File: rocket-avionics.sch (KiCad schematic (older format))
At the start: 20 parts

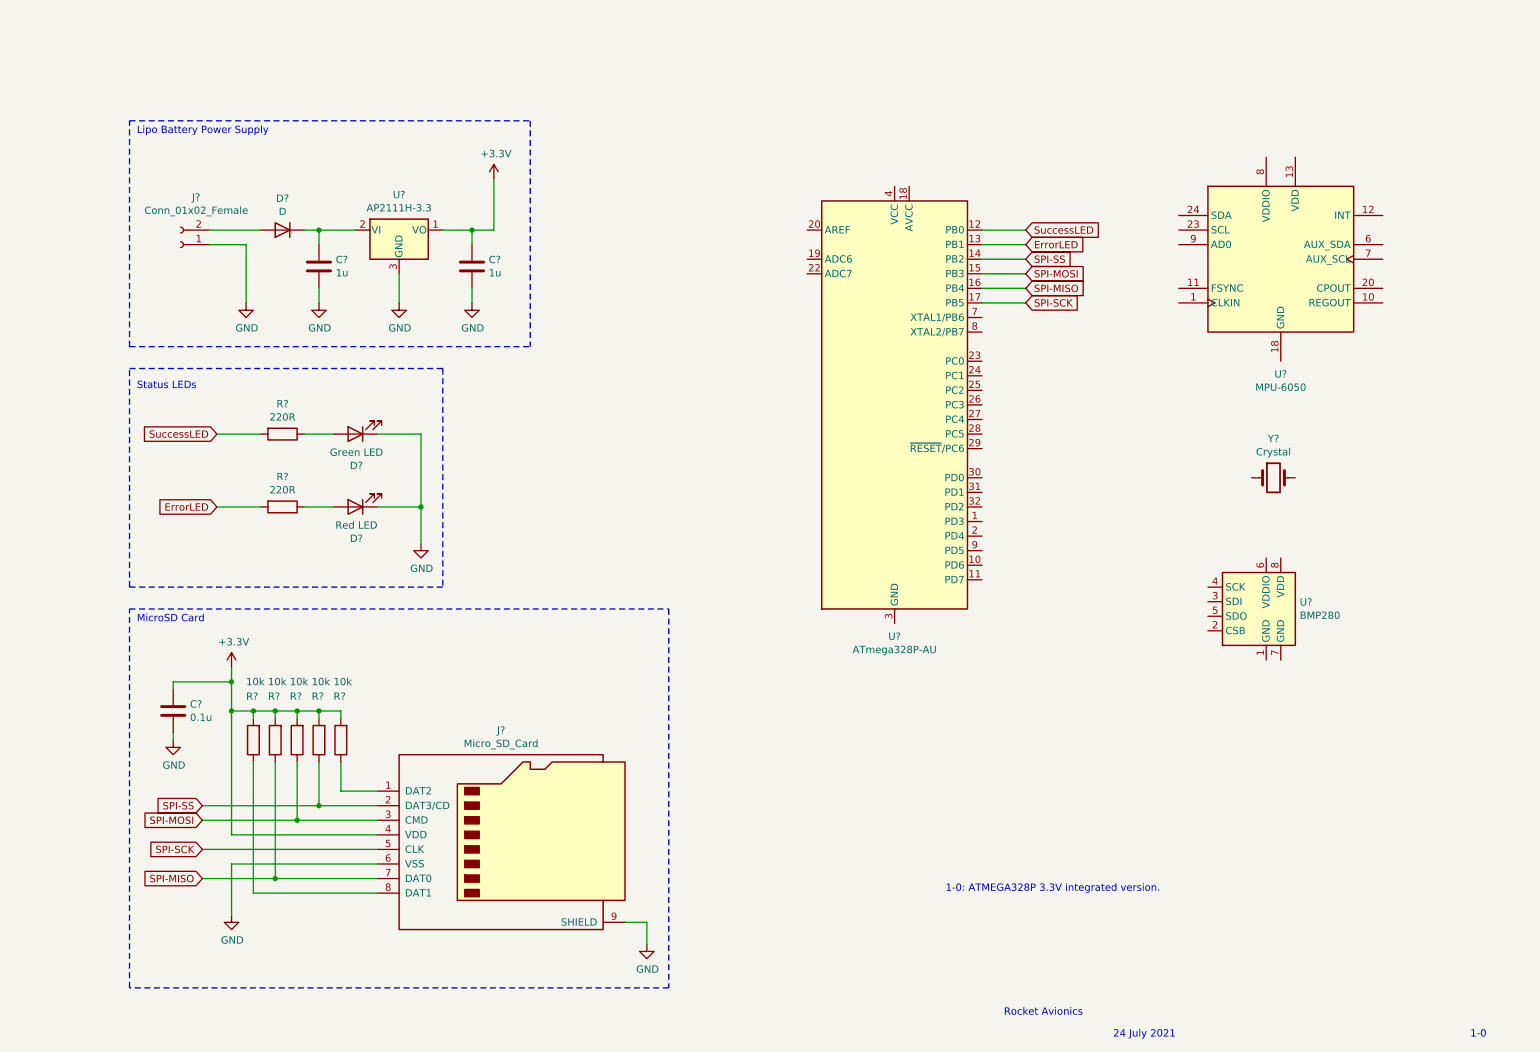
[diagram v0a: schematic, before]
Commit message: Complete MPU6050 section of schematic.
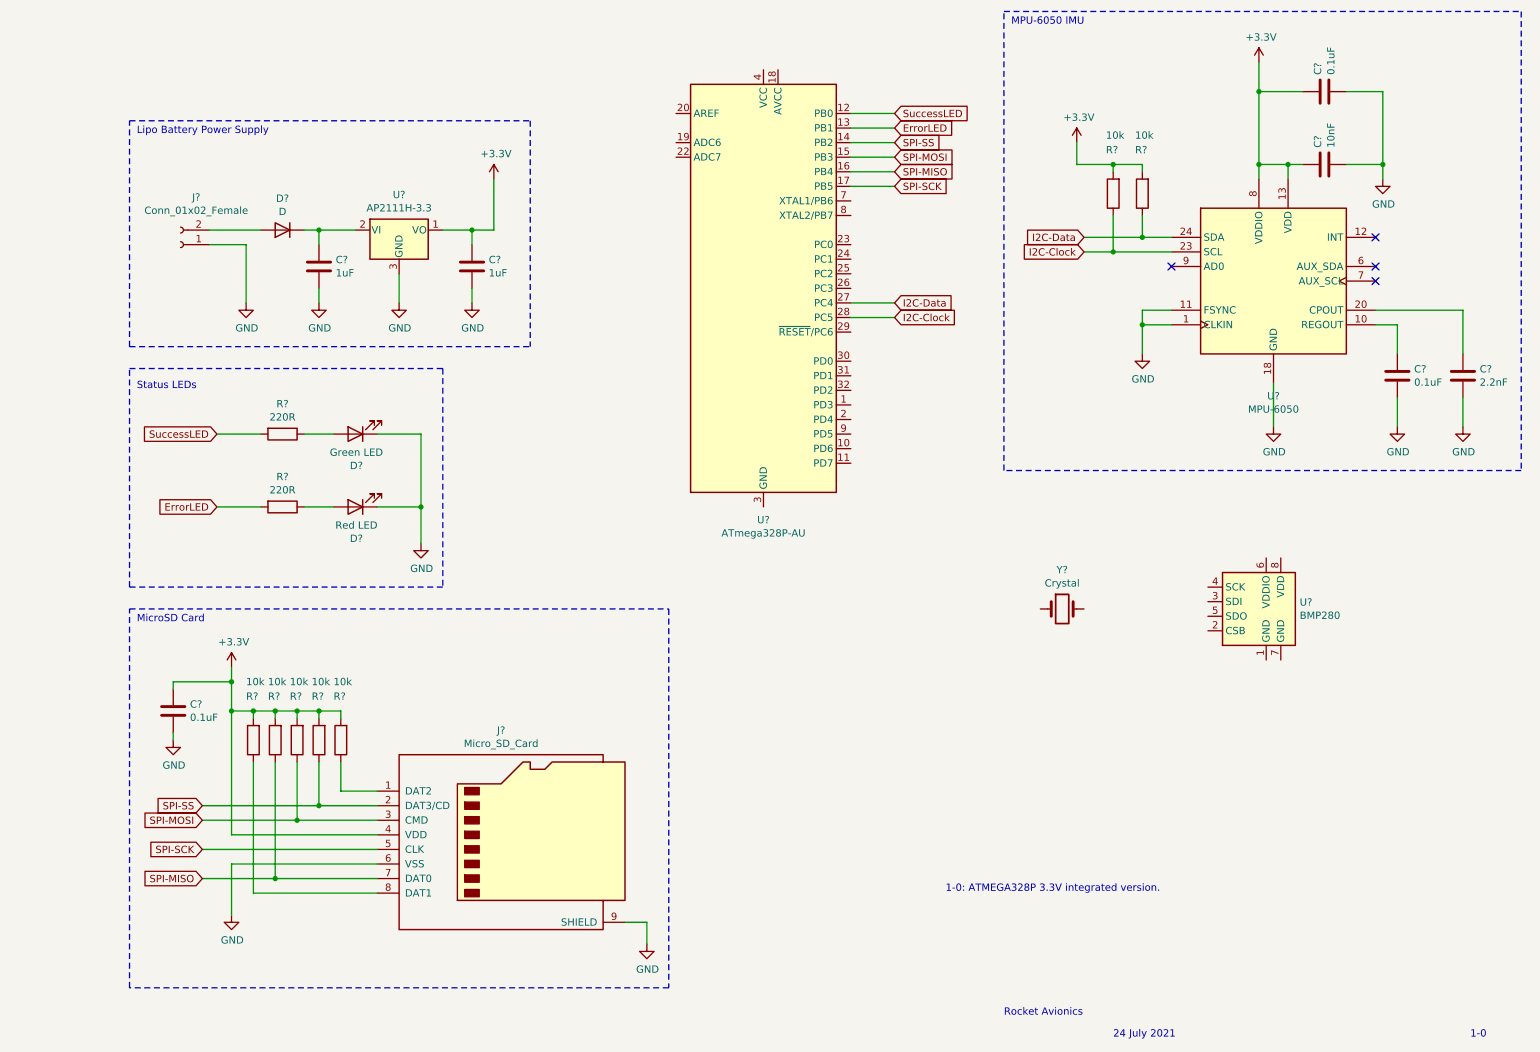
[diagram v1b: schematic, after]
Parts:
- added C?: 10nF, symbol Device:C
- added C? (x2): 0.1uF, symbol Device:C
- added C?: 2.2nF, symbol Device:C
- added R? (x2): 10k, symbol Device:R
- C?: value 0.1u -> 0.1uF
- C? (x2): value 1u -> 1uF
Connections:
- net +3V3: now also U?.13 (VDD), U?.8 (VDDIO), C?.1, C?.1, R?.2, R?.2
- net GND: now also U?.1 (CLKIN), U?.11 (FSYNC), U?.18 (GND), C?.2, C?.2, C?.2, C?.2
- net I2C-Data: now reaches U?.27 (PC4)
- net I2C-Data: now also U?.24 (SDA), R?.1
- net I2C-Clock: now reaches U?.28 (PC5)
- net I2C-Clock: now also U?.23 (SCL), R?.1
- net at U?.10 (REGOUT): now also C?.1
- net at U?.20 (CPOUT): now also C?.1
- no-connect marks 0 -> 4
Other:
- note added: "MPU-6050 IMU"
- moved on the sheet: U?, Y?

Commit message: Complete BMP280 section of schematic.
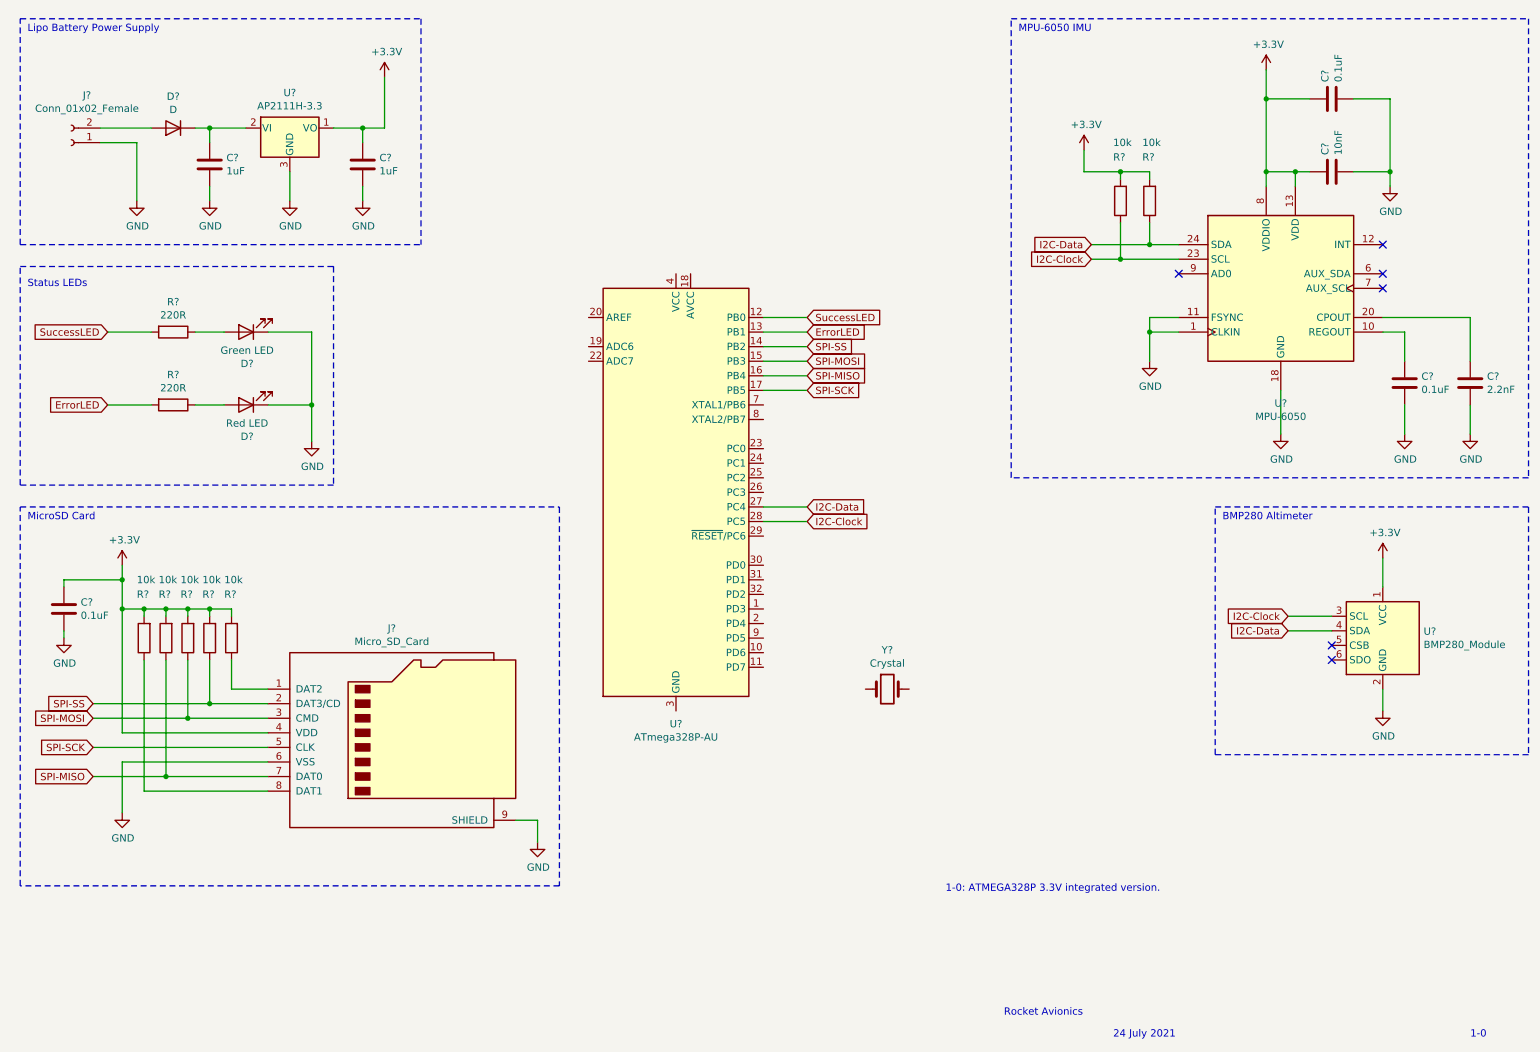
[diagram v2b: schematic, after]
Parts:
- removed U?: BMP280, Package_LGA:Bosch_LGA-8_2x2.5mm_P0.65mm_ClockwisePinNumbering, symbol Sensor_Pressure:BMP280
- added U?: BMP280_Module, Package_LGA:Bosch_LGA-8_2x2.5mm_P0.65mm_ClockwisePinNumbering, symbol rocket-avionics:BMP280_Module
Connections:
- net +3V3: now also U?.1 (VCC)
- net GND: now also U?.2 (GND)
- net I2C-Clock: now also U?.3 (SCL)
- net I2C-Data: now also U?.4 (SDA)
- no-connect marks 4 -> 6
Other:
- note added: "BMP280 Altimeter"
- moved on the sheet: C?, D?, J?, R?, U?, Y?

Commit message: Complete MCU section of schematic.
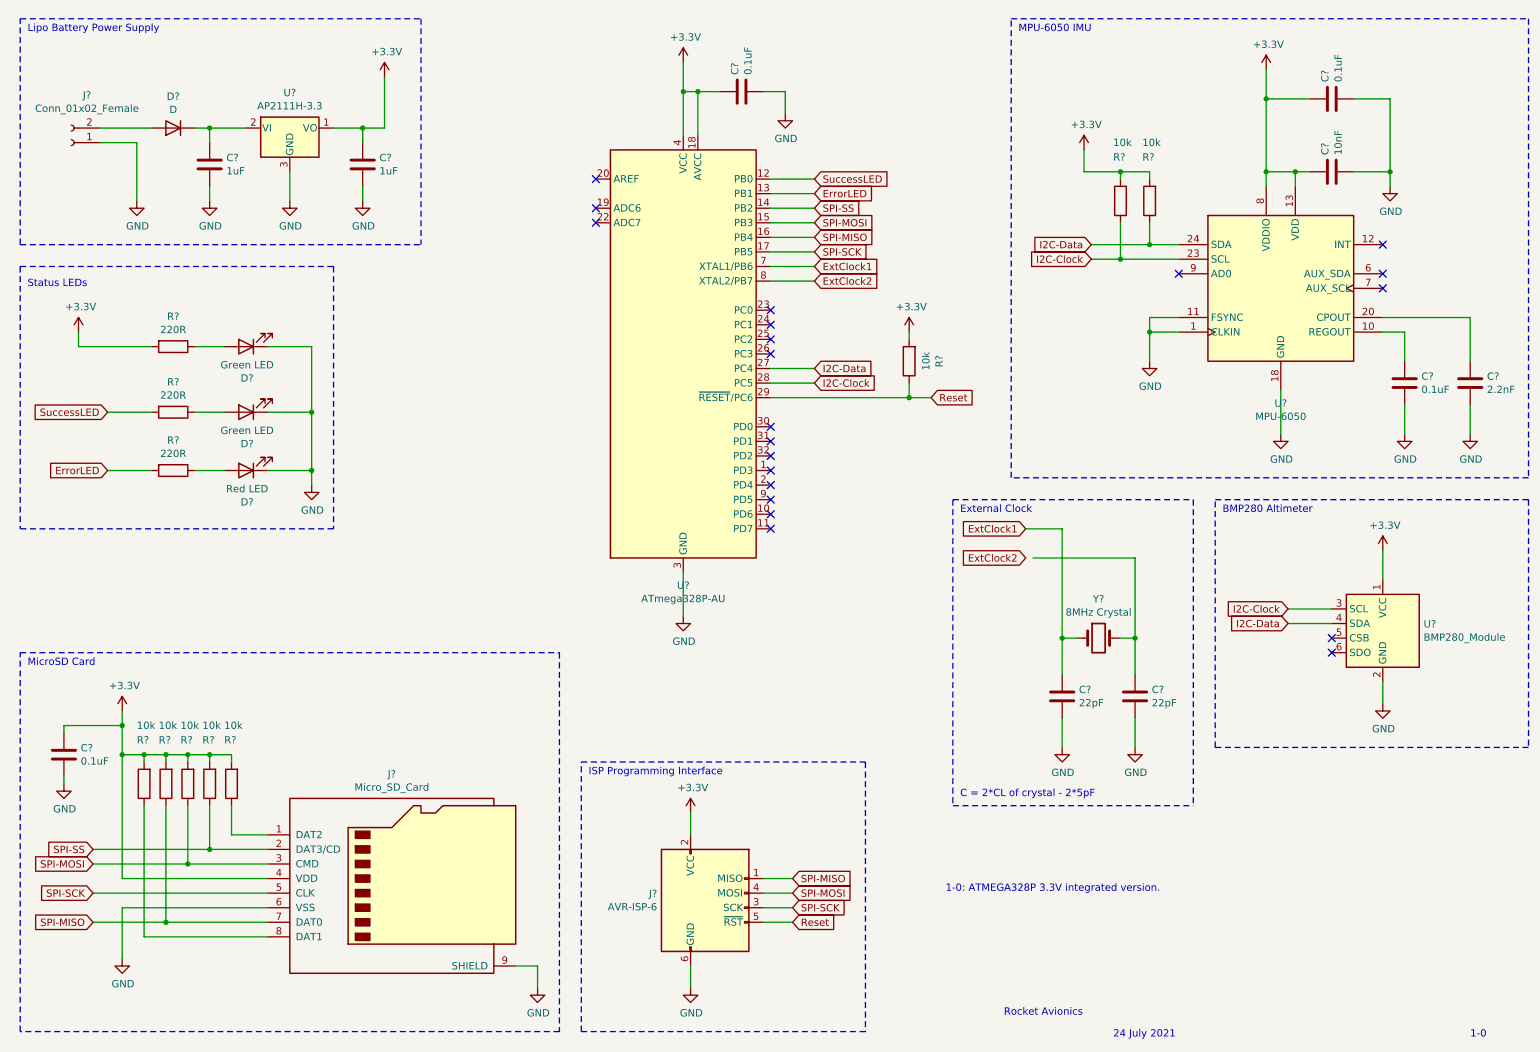
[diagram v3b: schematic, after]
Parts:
- added C? (x2): 22pF, symbol Device:C
- added C?: 0.1uF, symbol Device:C
- added D?: Green LED, symbol Device:LED
- added J?: AVR-ISP-6, symbol Connector:AVR-ISP-6
- added R?: 10k, symbol Device:R
- added R?: 220R, symbol Device:R
- Y?: value Crystal -> 8MHz Crystal
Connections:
- net +3V3: now also U?.18 (AVCC), U?.4 (VCC), U?.6 (VCC), C?.1, J?.2 (VCC), R?.2, R?.2
- net GND: now also U?.21 (GND), U?.3 (GND), U?.5 (GND), C?.2, C?.2, C?.2, D?.1 (K), J?.6 (GND)
- net SPI-MISO: now also J?.1 (MISO)
- net SPI-MOSI: now also J?.4 (MOSI)
- net SPI-SCK: now also J?.3 (SCK)
- net Reset: now reaches U?.29 (~RESET~/PC6)
- net Reset: now also J?.5 (~RST), R?.1
- net ExtClock1: now reaches U?.7 (XTAL1/PB6)
- net ExtClock1: now also Y?.1, C?.1
- net ExtClock2: now reaches U?.8 (XTAL2/PB7)
- net at Y?.2: now also C?.1
- new net: D?.2 (A), R?.1
- no-connect marks 6 -> 21
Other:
- note added: "C = 2*CL of crystal - 2*5pF"
- note added: "External Clock"
- note added: "ISP Programming Interface"
- moved on the sheet: C?, D?, J?, R?, U?, Y?

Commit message: Assign footprints to components in schematic.
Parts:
- C1, C10, C2, C3, C4, C5, C6, C7, C8, C9: renamed from C?; footprint (none) -> Capacitor_SMD:C_1206_3216Metric_Pad1.33x1.80mm_HandSolder
- D1: renamed from D?; value D -> MBR0520LT1; footprint (none) -> Diode_SMD:D_SOD-123
- D2, D3, D4: renamed from D?; footprint (none) -> LED_SMD:LED_1206_3216Metric_Pad1.42x1.75mm_HandSolder
- J1: renamed from J?; footprint (none) -> Connector_JST:JST_EH_B2B-EH-A_1x02_P2.50mm_Vertical
- J2: renamed from J?; footprint (none) -> electronics-rocket-avionics:microSD_HC_Hirose_DM3CS-SF
- J3: renamed from J?; footprint (none) -> electronics-rocket-avionics:AVR_ISP_2x3
- R1, R10, R11, R2, R3, R4, R5, R6, R7, R8, R9: renamed from R?; footprint (none) -> Resistor_SMD:R_1206_3216Metric_Pad1.30x1.75mm_HandSolder
- U1: renamed from U?; footprint (none) -> Package_TO_SOT_SMD:SOT-223; symbol Regulator_Linear:LM3480-3.3 -> Regulator_Linear:AMS1117-3.3
- U4: renamed from U?; footprint Package_LGA:Bosch_LGA-8_2x2.5mm_P0.65mm_ClockwisePinNumbering -> electronics-rocket-avionics:BMP280_Module
- Y1: renamed from Y?; footprint (none) -> Crystal:Crystal_SMD_HC49-SD_HandSoldering
- gave numbers to parts that had none: 2
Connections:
- net +3V3: now also U1.2 (VO); no longer U1.1 (VO)
- net GND: now also U1.1 (GND); no longer U1.3 (GND)
- net at C2.1, D1.1 (K): now also U1.3 (VI); no longer U1.2 (VI)
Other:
- note added: "CL of crystal = (C^2)/(2*C) + 5pF"
- note removed: "C = 2*CL of crystal - 2*5pF"

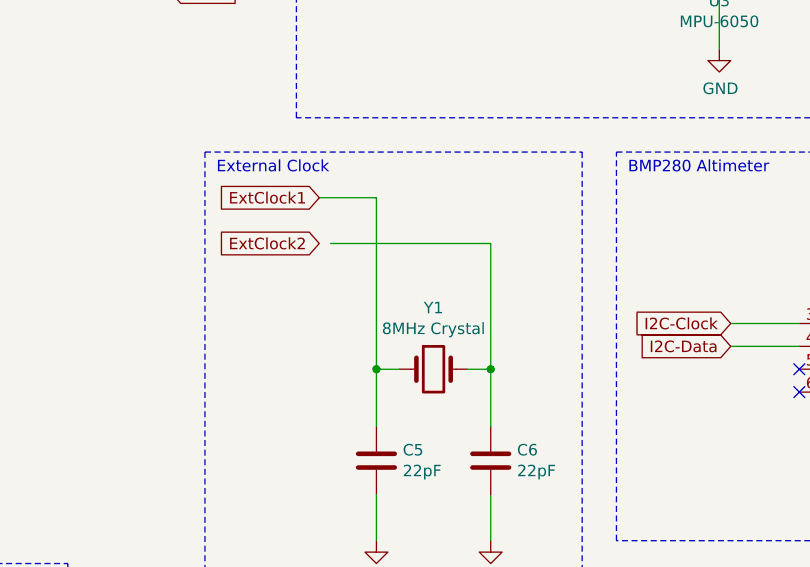
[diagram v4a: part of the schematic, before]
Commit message: Add traces and text to PCB layout.
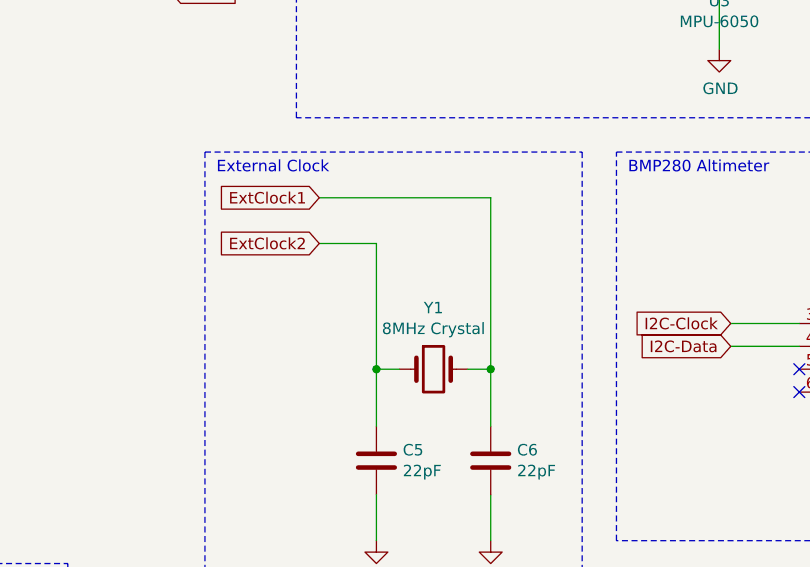
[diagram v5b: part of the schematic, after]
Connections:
- net ExtClock1: now also C6.1, Y1.2; no longer C5.1, Y1.1
- net ExtClock2: now also C5.1, Y1.1
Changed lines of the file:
@@
 $EndComp
 Wire Wire Line
-	7550 4150 7800 4150
-Wire Wire Line
-	7800 4150 7800 4900
+	7800 4350 7800 4900
 Wire Wire Line
 	7900 4900 7800 4900
@@
 Wire Wire Line
 	7800 4900 7800 5150
-Wire Wire Line
-	7600 4350 8300 4350
-Wire Wire Line
-	8300 4350 8300 4900
 Wire Wire Line
 	8200 4900 8300 4900
@@
 Wire Notes Line
 	4500 5750 6450 5750
+Wire Wire Line
+	7800 4350 7550 4350
+Wire Wire Line
+	7550 4150 8300 4150
+Wire Wire Line
+	8300 4150 8300 4900
 $EndSCHEMATC
